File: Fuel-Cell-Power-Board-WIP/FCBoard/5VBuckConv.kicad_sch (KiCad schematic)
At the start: 7 parts, among them U3 LM2576D2TR4-5G

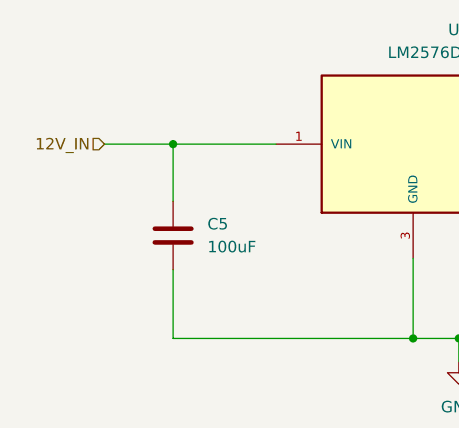
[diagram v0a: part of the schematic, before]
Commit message: Fixed some of the page names and corrected the voltage divider ratios for 12V and 5V voltage sensing.
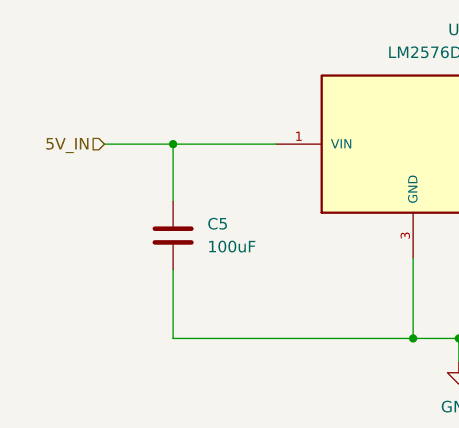
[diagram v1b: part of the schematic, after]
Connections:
- net 12V_IN renamed 5V_IN
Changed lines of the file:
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@@
     (effects (font (size 1.27 1.27)) (justify left))
   )
-  (hierarchical_label "12V_IN" (shape input) (at 52.07 88.9 180) (fields_autoplaced)
+  (hierarchical_label "5V_IN" (shape input) (at 52.07 88.9 180) (fields_autoplaced)
     (effects (font (size 1.27 1.27)) (justify right))
   )
